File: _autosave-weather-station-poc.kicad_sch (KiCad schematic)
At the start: 0 parts

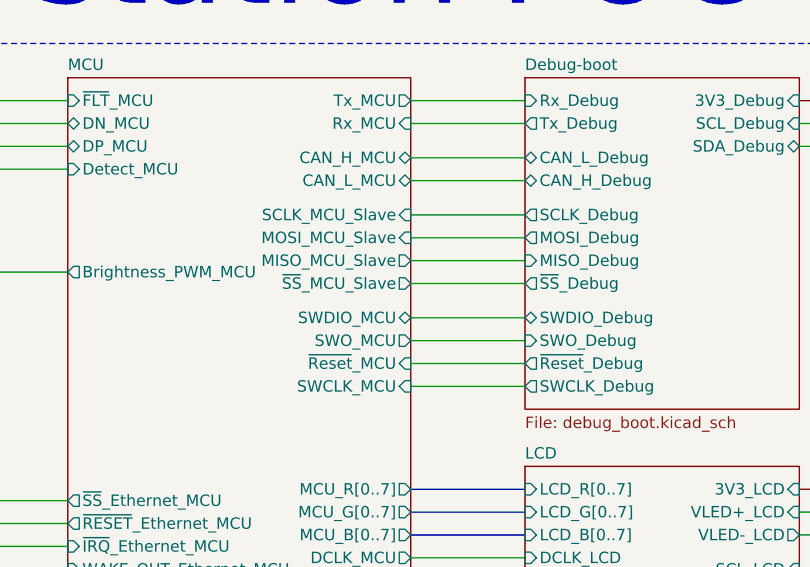
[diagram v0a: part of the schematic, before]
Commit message: Fix errors in synoptic and hierarchic pins
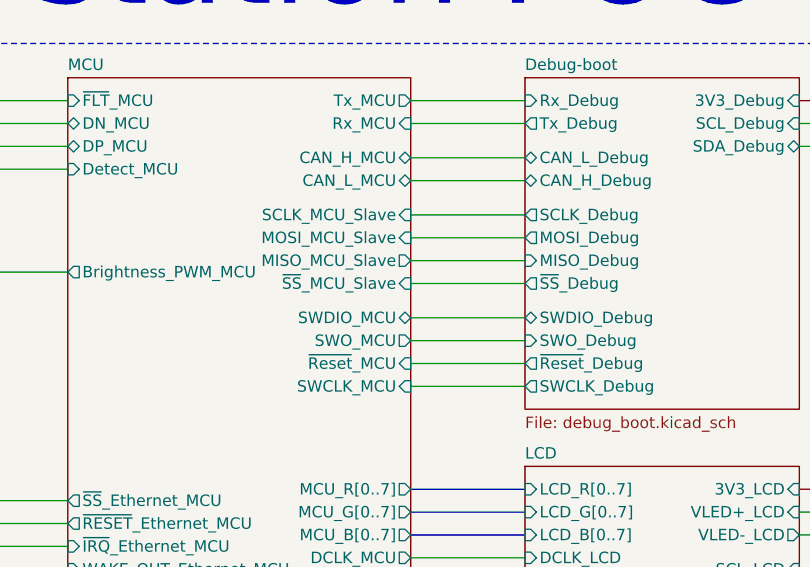
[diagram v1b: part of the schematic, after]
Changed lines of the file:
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@@
-			)
-		)
-		(pin "~{SS}_MCU_Slave" output
-			(at 181.61 59.69 0)
-			(effects
-				(font
-					(size 1.27 1.27)
-				)
-				(justify right)
 			)
 		)
@@
 			)
 		)
+		(pin "~{SS}_MCU_Slave" input
+			(at 181.61 59.69 0)
+			(effects
+				(font
+					(size 1.27 1.27)
+				)
+				(justify right)
+			)
+		)
